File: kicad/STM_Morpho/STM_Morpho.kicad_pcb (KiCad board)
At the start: 2 copper layers, 69.8 x 68.5 mm, 6 parts, among them CN10 CONN_02X19, CN7 CONN_02X19, J1 Conn_GameBoy_Cartridge_Slot, SW1 SW_SPDT, SW2 SW_SPST

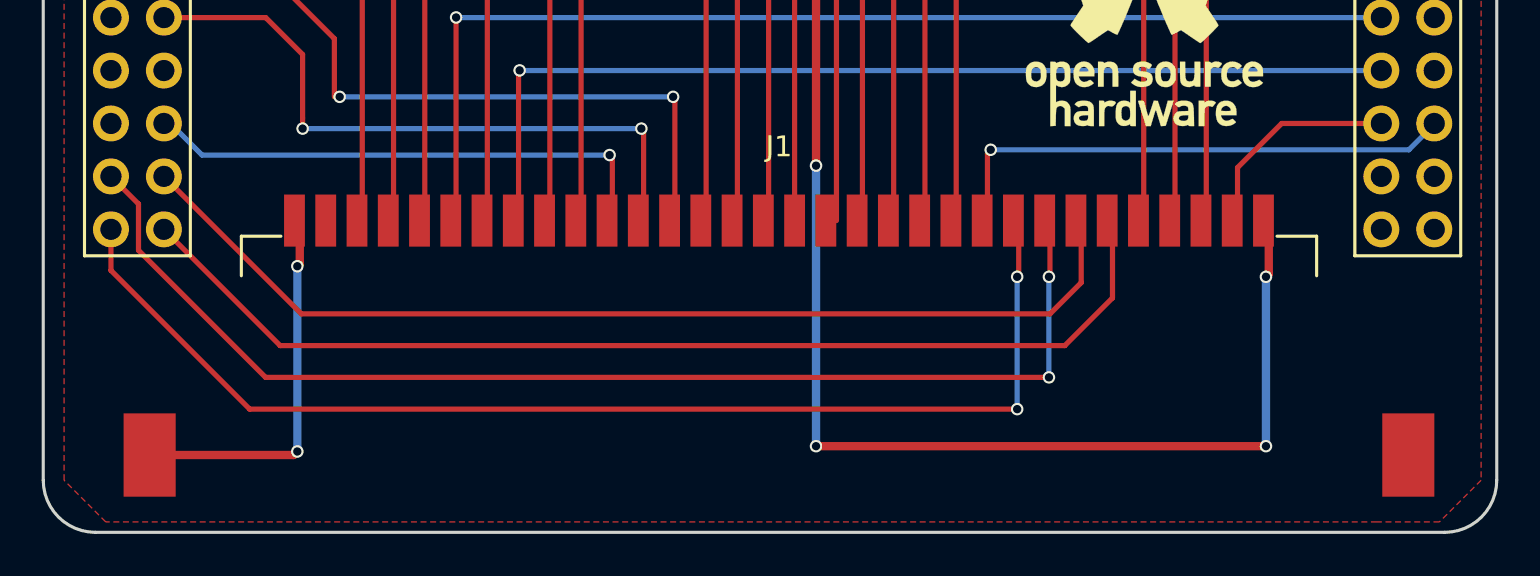
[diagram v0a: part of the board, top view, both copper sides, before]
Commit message: Use submodule for Gekkio Kicad libs
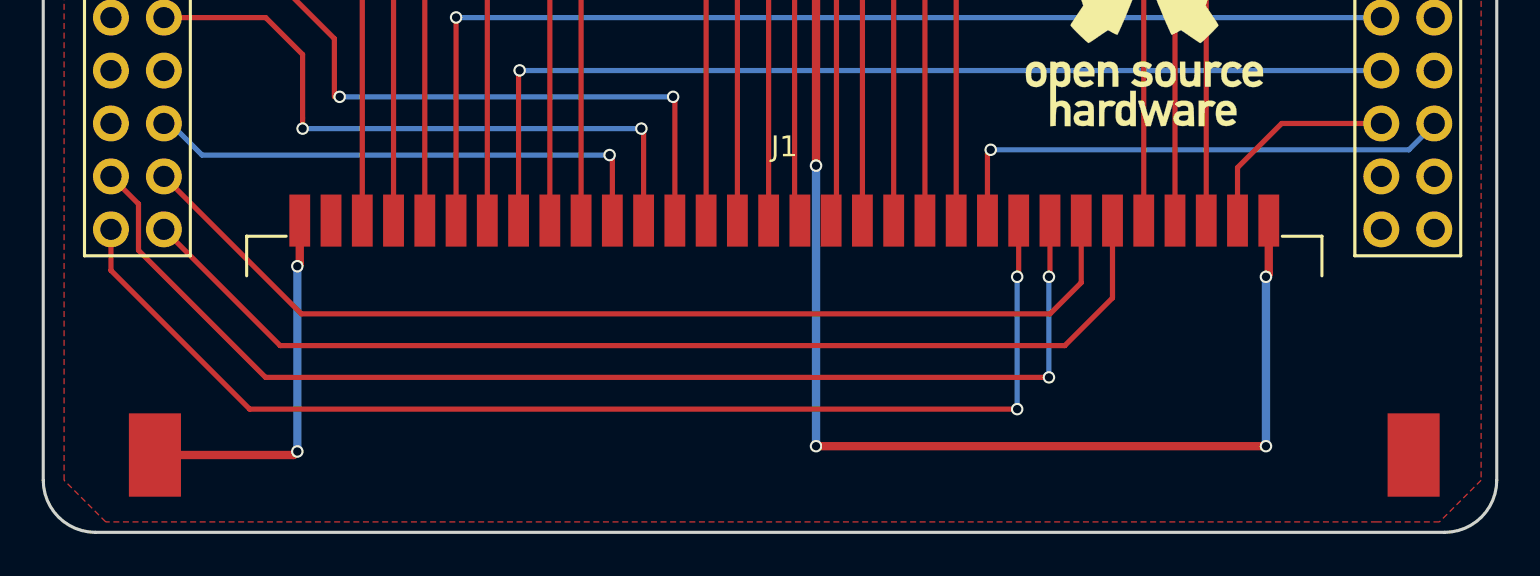
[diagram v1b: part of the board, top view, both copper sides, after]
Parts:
- moved J1 0.25 mm to (165.6, 122.5)
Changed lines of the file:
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@@
   (general
     (links 41)
-    (no_connects 1)
+    (no_connects 0)
     (area 129.924999 62.924999 199.825001 131.575001)
     (thickness 1.6)
@@
   )
   (module Gekkio_GameBoy:GameBoy_Cartridge_Slot_DSLite (layer F.Cu)
-    (at 165.306 122.54 180)
+    (at 165.56 122.54 180)
     (descr "Game Boy cartridge slot, DS Lite")
     (tags "gameboy cartridge slot")

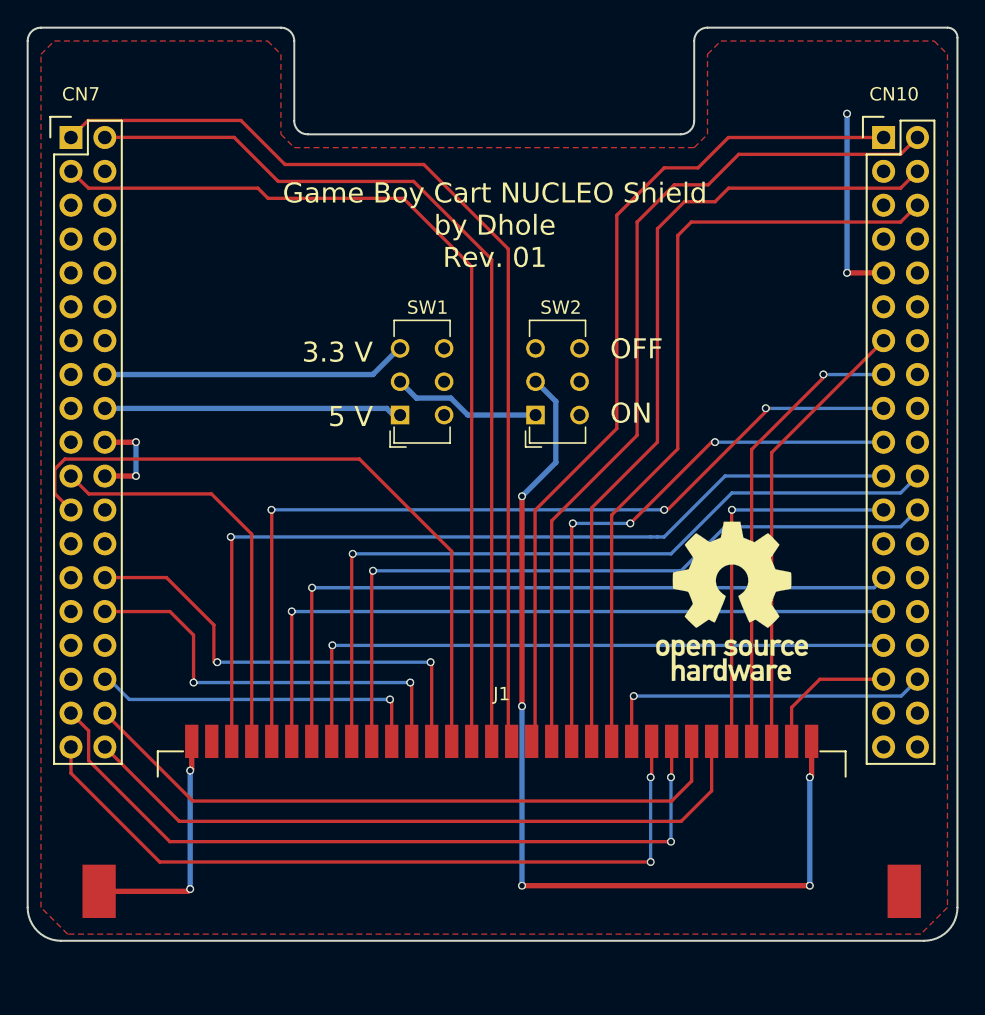
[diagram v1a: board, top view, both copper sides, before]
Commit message: Use different GBA cart slot
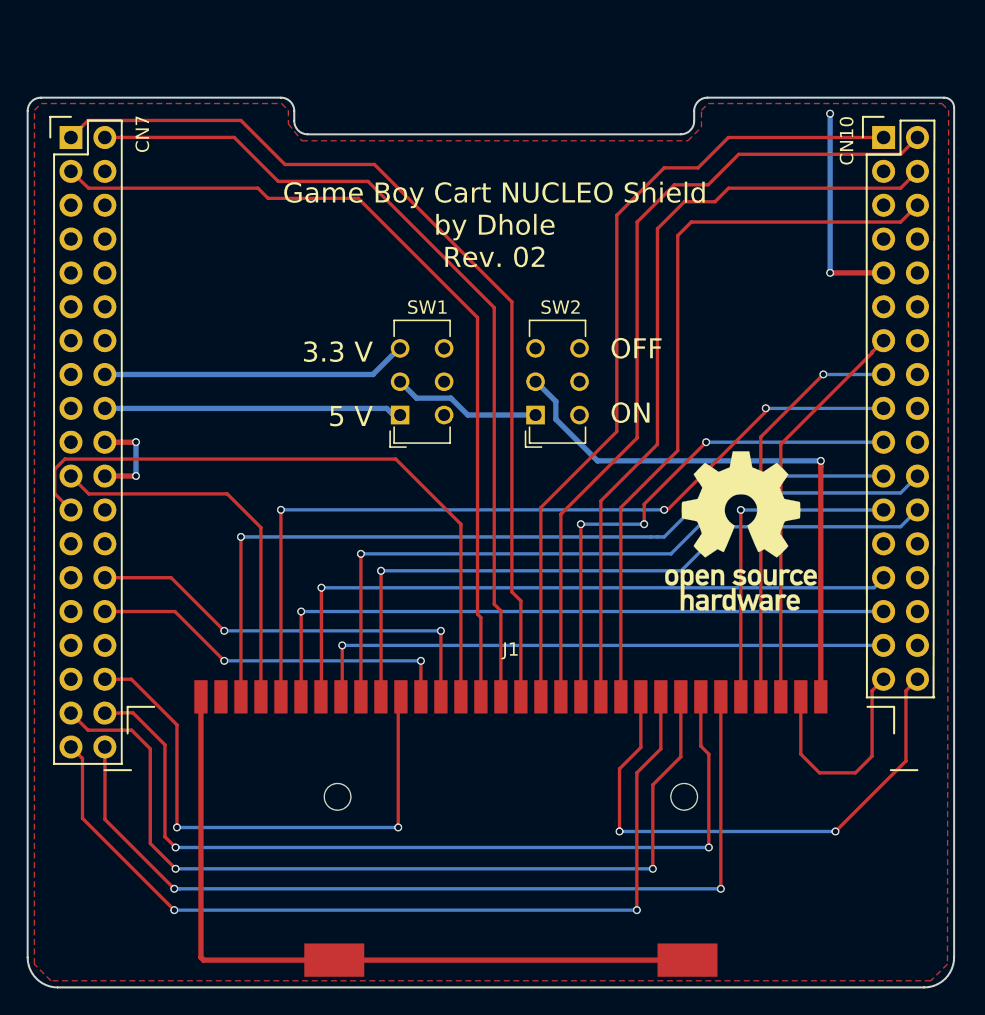
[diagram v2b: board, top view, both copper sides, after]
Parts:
- CN10: footprint Pin_Headers:Pin_Header_Straight_2x19 -> STM_Morpho:Pin_Header_Straight_2x17
- J1: footprint Gekkio_GameBoy:GameBoy_Cartridge_Slot_DSLite -> STM_Morpho:GameBoy_Cartridge_Slot_NDS
- moved J1 29.5 mm to (138.0, 112.0)
- moved REF*** 5.32 mm to (183.5, 100.8)
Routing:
- net GND: track 37.7 -> 77.1 mm, vias 6 -> 4
- net VCC: track 72.5 -> 42.8 mm, vias 5 -> 1
- net D0: track 25.2 -> 41.3 mm, vias 1 -> 2
- net A0: track 52.5 -> 68.2 mm, vias 0 -> 2
- net A4: track 25.3 -> 41.0 mm, vias 1 -> 2
- net A1: track 50.4 -> 65.1 mm, vias 0 -> 2
- net A3: track 57.3 -> 66.9 mm
- net A2: track 57.9 -> 66.4 mm
- net CLK: track 10.3 -> 16.9 mm
- net A10: track 74.3 -> 69.1 mm
- net A11: track 69.0 -> 63.9 mm
- net A12: track 68.6 -> 63.6 mm
- net /RES: track 66.2 -> 62.1 mm
- net D3: track 48.6 -> 44.5 mm
- net D6: track 66.5 -> 62.4 mm
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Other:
- board size 69.8 x 68.5 mm -> 69.5 x 66.8 mm
- board text added: "Game Boy Cart NUCLEO Shield by Dhole Rev. 02"
- board text removed: "Game Boy Cart NUCLEO Shield by Dhole Rev. 01"
